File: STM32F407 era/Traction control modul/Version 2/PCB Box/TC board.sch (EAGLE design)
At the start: 121 parts, among them IC1 74HC14D, IC2 lm2575, IC5 REG1117, J1 CON1, J2 CON1, U1 MAX13052ESA+, U2 MAX232AEWE+, U3 MAX531AESD+

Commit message: finished RC
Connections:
- new net AUX1: J1G$1.D, U$1G$1.PE9
- new net AUX6: J2G$1.E, U$1G$4.PE4
- new net AUX7: J2G$3.E, U$1G$4.PE5
- net 3.3V: no longer J1G$2.D
- net BRAKEP: now also J2G$4.F; no longer J2G$3.H
- net GEARPOSAN: now also J2G$3.H; no longer J2G$4.F
- net GND: now also J1G$2.D, J2G$2.E, J2G$4.E; no longer J1G$1.D
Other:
- note added: "RS232 Debug"
- moved on the sheet: C13, J1G$1, J1G$2, J1G$3, J1G$4, J2G$1, J2G$2, J2G$3, J2G$4, JP1, Q10, Q11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

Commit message: continued work
started work on wireless lap timer with LoRa
added RS232 and USB-UART to com node
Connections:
- net COM2RX: now also U2.R1OUT; no longer U2.T1OUT
- net DRS232TX: now also U2.T1OUT; no longer U2.R1OUT
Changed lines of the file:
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@@
 <net name="COM2RX" class="0">
-<segment>
-<pinref part="U2" gate="A" pin="T1OUT"/>
-<wire x1="-142.24" y1="55.88" x2="-144.78" y2="55.88" width="0.1524" layer="91"/>
-<label x="-142.24" y="55.88" size="1.27" layer="95" xref="yes"/>
-</segment>
 <segment>
 <pinref part="U$1" gate="G$3" pin="PC11"/>
 <wire x1="-48.26" y1="-17.78" x2="-50.8" y2="-17.78" width="0.1524" layer="91"/>
 <label x="-48.26" y="-17.78" size="1.27" layer="95" xref="yes"/>
+</segment>
+<segment>
+<pinref part="U2" gate="A" pin="R1OUT"/>
+<wire x1="-142.24" y1="48.26" x2="-144.78" y2="48.26" width="0.1524" layer="91"/>
+<label x="-142.24" y="48.26" size="1.27" layer="95" xref="yes"/>
 </segment>
 </net>
@@
 <net name="DRS232TX" class="0">
 <segment>
-<pinref part="U2" gate="A" pin="R1OUT"/>
-<wire x1="-142.24" y1="48.26" x2="-144.78" y2="48.26" width="0.1524" layer="91"/>
-<label x="-142.24" y="48.26" size="1.27" layer="95" xref="yes"/>
-</segment>
-<segment>
 <pinref part="JP1" gate="G$1" pin="3"/>
 <wire x1="-111.76" y1="55.88" x2="-109.22" y2="55.88" width="0.1524" layer="91"/>
 <label x="-111.76" y="55.88" size="1.27" layer="95" rot="R180" xref="yes"/>
 </segment>
+<segment>
+<pinref part="U2" gate="A" pin="T1OUT"/>
+<wire x1="-142.24" y1="55.88" x2="-144.78" y2="55.88" width="0.1524" layer="91"/>
+<label x="-142.24" y="55.88" size="1.27" layer="95" xref="yes"/>
+</segment>
 </net>

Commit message: All boards RC done!
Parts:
- removed JP1: (no value), SparkFun-Connectors:DB9FEMALE
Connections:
- removed net COM2RX: U$1G$3.PC11, U2.R1OUT
- removed net COM2TX: U$1G$3.PC10, U2.T1IN
- removed net DRS232RX: JP1.2, U2.R1IN
- removed net DRS232TX: JP1.3, U2.T1OUT
- net GND: no longer JP1.5
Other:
- note removed: "RS232 Debug"
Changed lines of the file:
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@@
 <part name="GND58" library="supply1" deviceset="GND" device=""/>
 <part name="GND59" library="supply1" deviceset="GND" device=""/>
-<part name="JP1" library="SparkFun-Connectors" deviceset="DB9" device="FEMALE"/>
-<part name="GND60" library="supply1" deviceset="GND" device=""/>
 </parts>
 <sheets>
@@
 <wire x1="88.9" y1="38.1" x2="88.9" y2="-5.08" width="0.3048" layer="97"/>
 <wire x1="88.9" y1="-5.08" x2="-127" y2="-5.08" width="0.3048" layer="97"/>
-<wire x1="-127" y1="71.12" x2="-83.82" y2="71.12" width="0.3048" layer="97"/>
-<wire x1="-83.82" y1="71.12" x2="-83.82" y2="40.64" width="0.3048" layer="97"/>
-<wire x1="-83.82" y1="40.64" x2="-127" y2="40.64" width="0.3048" layer="97"/>
-<wire x1="-127" y1="40.64" x2="-127" y2="71.12" width="0.3048" layer="97"/>
-<text x="-124.46" y="68.58" size="1.778" layer="97" font="vector">RS232 Debug</text>
 </plain>
 <instances>
@@
 <instance part="GND58" gate="1" x="388.62" y="12.7"/>
 <instance part="GND59" gate="1" x="396.24" y="12.7"/>
-<instance part="JP1" gate="G$1" x="-101.6" y="55.88"/>
-<instance part="GND60" gate="1" x="-111.76" y="45.72"/>
 </instances>
 <busses>
@@
 <pinref part="GND59" gate="1" pin="GND"/>
 </segment>
-<segment>
-<pinref part="JP1" gate="G$1" pin="5"/>
-<pinref part="GND60" gate="1" pin="GND"/>
-<wire x1="-109.22" y1="50.8" x2="-111.76" y2="50.8" width="0.1524" layer="91"/>
-<wire x1="-111.76" y1="50.8" x2="-111.76" y2="48.26" width="0.1524" layer="91"/>
-</segment>
 </net>
 <net name="3.3V" class="0">
@@
 </segment>
 </net>
-<net name="COM2TX" class="0">
-<segment>
-<pinref part="U2" gate="A" pin="T1IN"/>
-<wire x1="-182.88" y1="48.26" x2="-180.34" y2="48.26" width="0.1524" layer="91"/>
-<label x="-182.88" y="48.26" size="1.27" layer="95" rot="R180" xref="yes"/>
-</segment>
-<segment>
-<pinref part="U$1" gate="G$3" pin="PC10"/>
-<wire x1="-76.2" y1="-17.78" x2="-73.66" y2="-17.78" width="0.1524" layer="91"/>
-<label x="-76.2" y="-17.78" size="1.27" layer="95" rot="R180" xref="yes"/>
-</segment>
-</net>
-<net name="COM2RX" class="0">
-<segment>
-<pinref part="U$1" gate="G$3" pin="PC11"/>
-<wire x1="-48.26" y1="-17.78" x2="-50.8" y2="-17.78" width="0.1524" layer="91"/>
-<label x="-48.26" y="-17.78" size="1.27" layer="95" xref="yes"/>
-</segment>
-<segment>
-<pinref part="U2" gate="A" pin="R1OUT"/>
-<wire x1="-142.24" y1="48.26" x2="-144.78" y2="48.26" width="0.1524" layer="91"/>
-<label x="-142.24" y="48.26" size="1.27" layer="95" xref="yes"/>
-</segment>
-</net>
-<net name="DRS232RX" class="0">
-<segment>
-<pinref part="U2" gate="A" pin="R1IN"/>
-<wire x1="-182.88" y1="40.64" x2="-180.34" y2="40.64" width="0.1524" layer="91"/>
-<label x="-182.88" y="40.64" size="1.27" layer="95" rot="R180" xref="yes"/>
-</segment>
-<segment>
-<pinref part="JP1" gate="G$1" pin="2"/>
-<wire x1="-111.76" y1="58.42" x2="-109.22" y2="58.42" width="0.1524" layer="91"/>
-<label x="-111.76" y="58.42" size="1.27" layer="95" rot="R180" xref="yes"/>
-</segment>
-</net>
-<net name="DRS232TX" class="0">
-<segment>
-<pinref part="JP1" gate="G$1" pin="3"/>
-<wire x1="-111.76" y1="55.88" x2="-109.22" y2="55.88" width="0.1524" layer="91"/>
-<label x="-111.76" y="55.88" size="1.27" layer="95" rot="R180" xref="yes"/>
-</segment>
-<segment>
-<pinref part="U2" gate="A" pin="T1OUT"/>
-<wire x1="-142.24" y1="55.88" x2="-144.78" y2="55.88" width="0.1524" layer="91"/>
-<label x="-142.24" y="55.88" size="1.27" layer="95" xref="yes"/>
-</segment>
-</net>
 <net name="AUX1" class="0">
 <segment>
@@
 </sheet>
 </sheets>
+<errors>
+</errors>
 </schematic>
 </drawing>

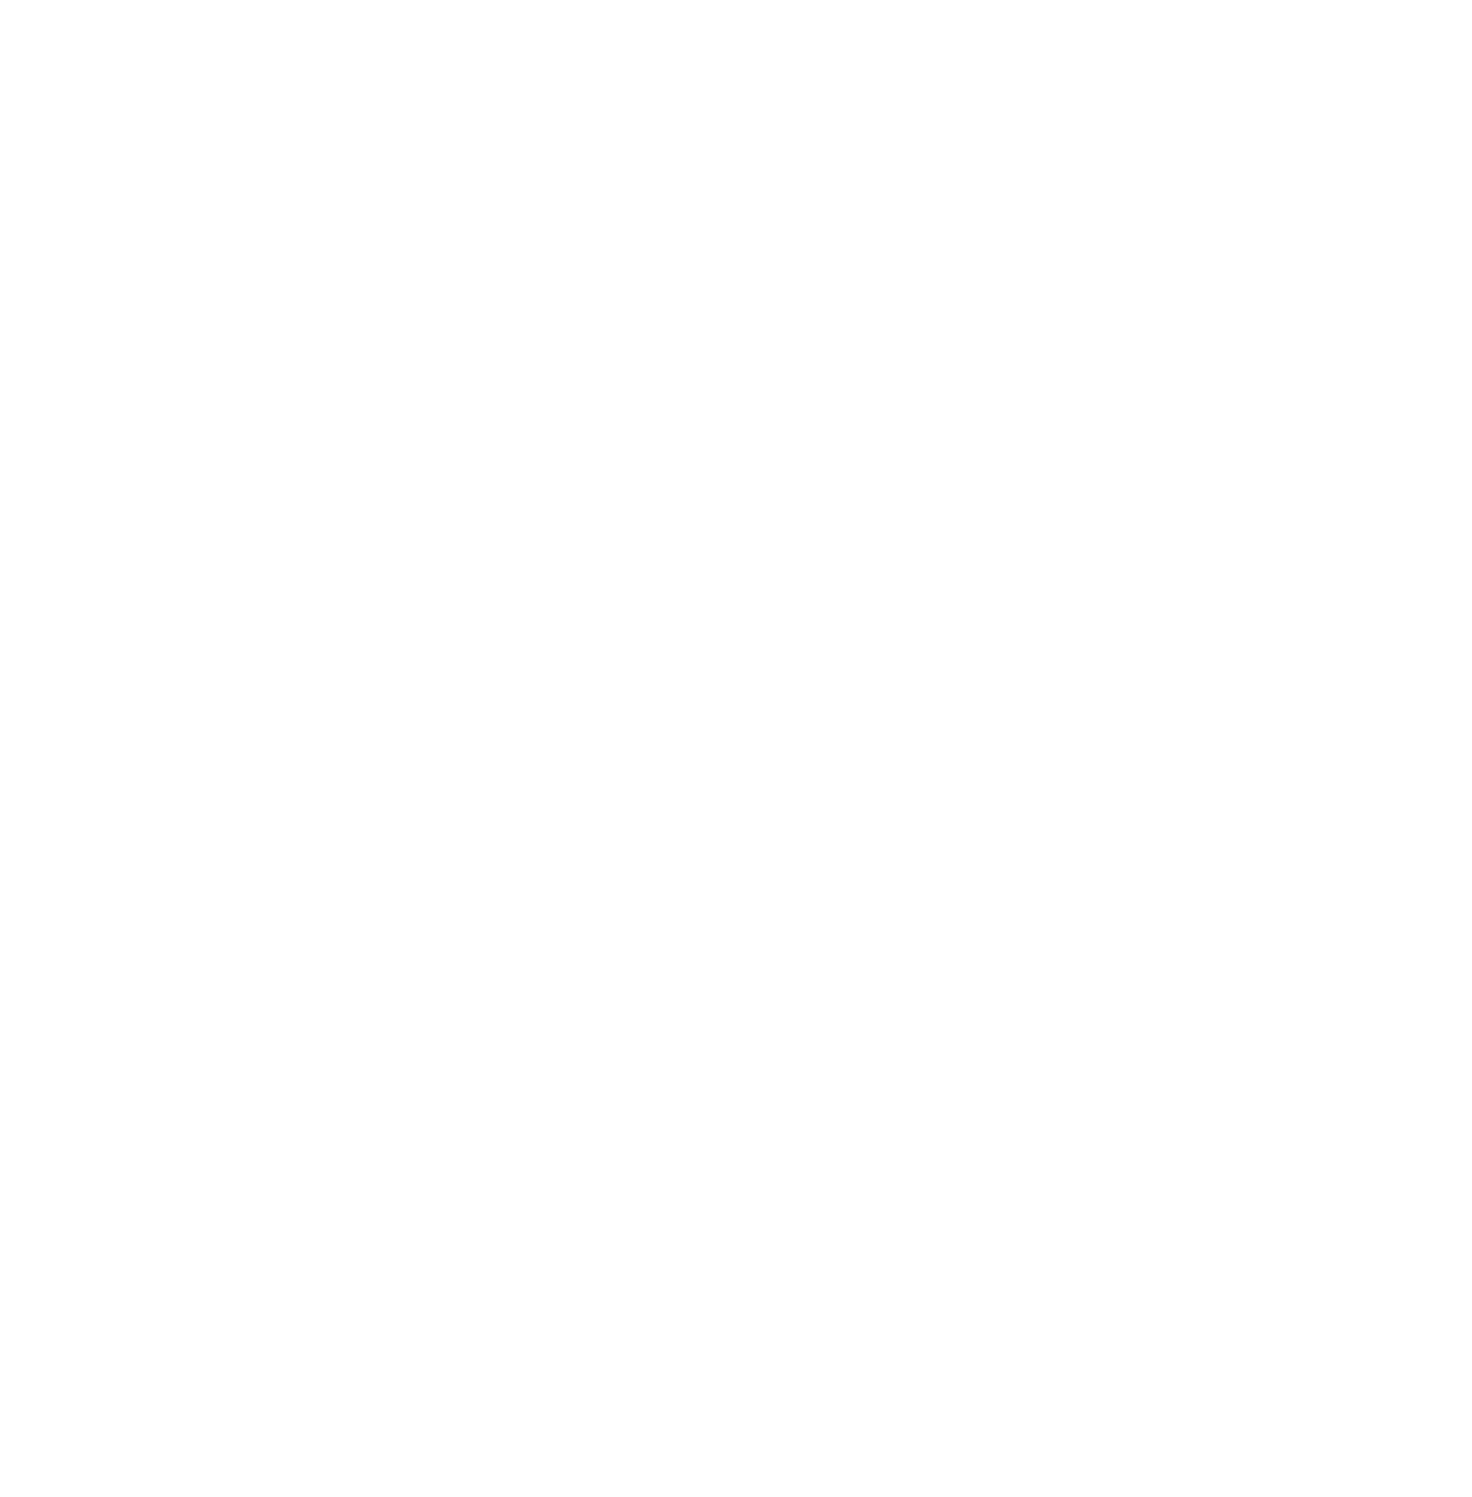
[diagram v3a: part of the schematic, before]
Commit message: added correct wheel speed sensor ic's and buffer
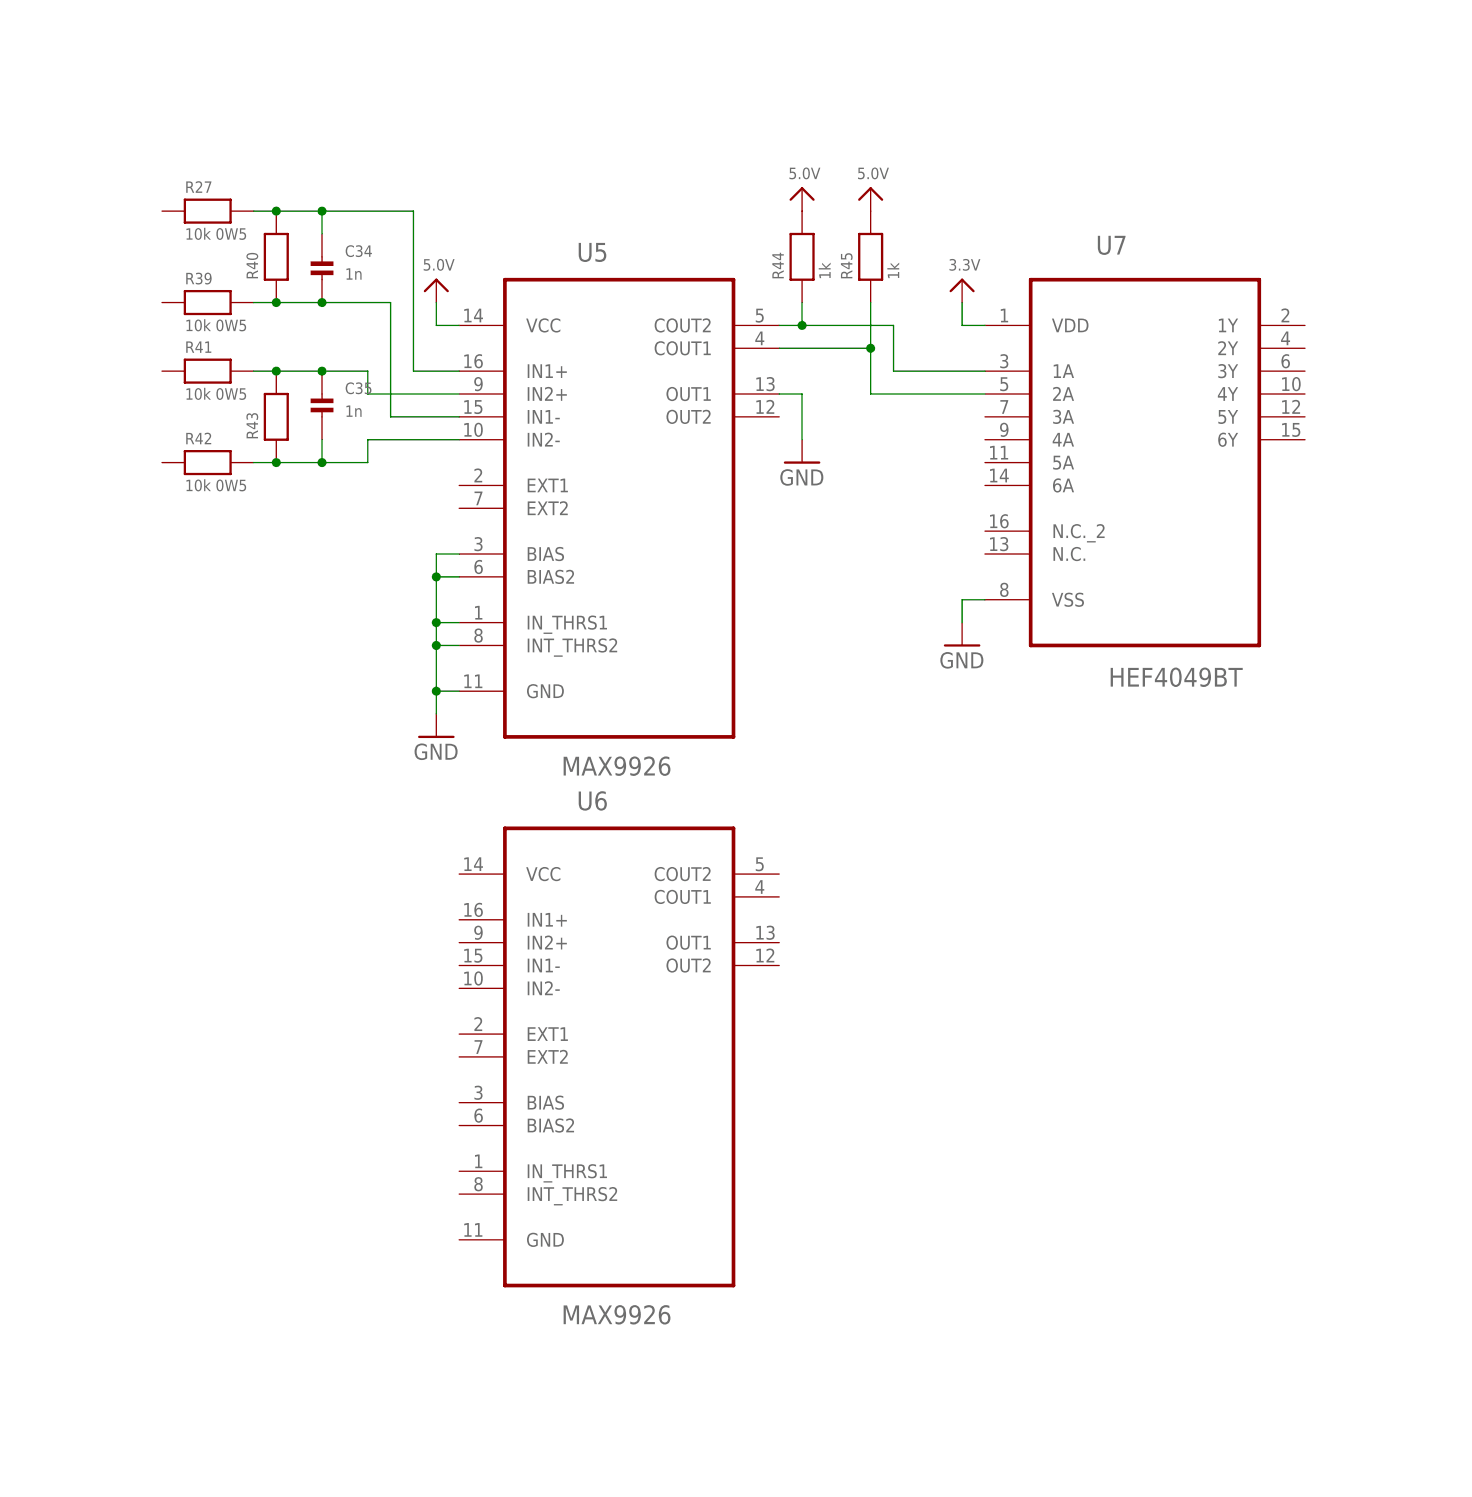
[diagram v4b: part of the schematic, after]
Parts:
- added C34, C35: 1n, microbuilder:CAP_CERAMIC_0603
- added R27, R39, R41, R42: 10k 0W5, microbuilder:RESISTOR_0805
- added R40, R43: (no value), microbuilder:RESISTOR_0805
- added R44, R45: 1k, microbuilder:RESISTOR_0603
- added U5, U6: MAX9926, Maxim_By_element14_Batch_1:MAX9927AEE+
- added U7: HEF4049BT, NXP_By_element14_Batch_1:HEF4049BT
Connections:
- new net N$11: C34.P$1, R27.2, R40.2, U5.IN1+
- new net N$15: C34.P$2, R39.2, R40.1, U5.IN1-
- new net N$17: C35.P$1, R41.2, R43.2, U5.IN2+
- new net N$18: C35.P$2, R42.2, R43.1, U5.IN2-
- new net N$28: R44.1, U5.COUT2, U7.1A
- new net N$31: R45.1, U5.COUT1, U7.2A
- net 3.3V: now also U7.VDD
- net 5.0V: now also R44.2, R45.2, U5.VCC
- net GND: now also U5.BIAS, U5.BIAS2, U5.GND, U5.INT_THRS2, U5.IN_THRS1, U5.OUT1, U7.VSS

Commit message: more work on wheel speed sensor IC
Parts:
- removed IC1: 74HC14D, 74xx-eu:74HC14D
- added C36, C37: 1n, microbuilder:CAP_CERAMIC_0603
- added C38, C39: 100n, microbuilder:CAP_CERAMIC_0603
- added R46, R47: 1k, microbuilder:RESISTOR_0603
- added R48, R49, R51, R52: 10k 0W5, microbuilder:RESISTOR_0805
- added R50, R53: (no value), microbuilder:RESISTOR_0805
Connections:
- new net N$29: R46.1, U6.COUT2, U7.3A
- new net N$33: R47.1, U6.COUT1, U7.4A
- new net N$36: C36.P$1, R48.2, R50.2, U6.IN1+
- new net N$39: C37.P$1, R51.2, R53.2, U6.IN2+
- new net N$40: C37.P$2, R52.2, R53.1, U6.IN2-
- new net N$41: C36.P$2, R49.2, R50.1, U6.IN1-
- new net RPM1GIN: J2G$4.B, R42.1
- new net RPM2GIN: J2G$3.B, R27.1
- new net RPM3GIN: J2G$2.B, R52.1
- new net RPM4GIN: J2G$1.B, R48.1
- net 3.3V: no longer IC1P.VCC
- net 5.0V: now also C38.P$1, C39.P$1, R46.2, R47.2, U6.VCC
- net GND: now also C38.P$2, C39.P$2, U6.BIAS, U6.BIAS2, U6.GND, U6.INT_THRS2, U6.IN_THRS1, U6.OUT1; no longer IC1E.I, IC1F.I, IC1P.GND, J2G$1.B, J2G$2.B, J2G$3.B, J2G$4.B
- net RPM1: now also U7.4Y; no longer IC1D.O
- net RPM1IN: now also R41.1; no longer IC1D.I
- net RPM2: now also U7.3Y; no longer IC1C.O
- net RPM2IN: now also J2G$3.A, R39.1; no longer IC1C.I, J2G$1.A
- net RPM3: now also U7.2Y; no longer IC1B.O
- net RPM3IN: now also R51.1; no longer IC1B.I
- net RPM4: now also U7.1Y; no longer IC1A.O
- net RPM4IN: now also J2G$1.A, R49.1; no longer IC1A.I, J2G$3.A
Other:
- note removed: "Connector 1"
- moved on the sheet: C3, C34, C35, R27, R39, R40, R41, R42, R43, R44, R45, U5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
